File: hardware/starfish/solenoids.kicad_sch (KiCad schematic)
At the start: 8 parts, among them J1201 Solenoid, U1201 DRV120PWR

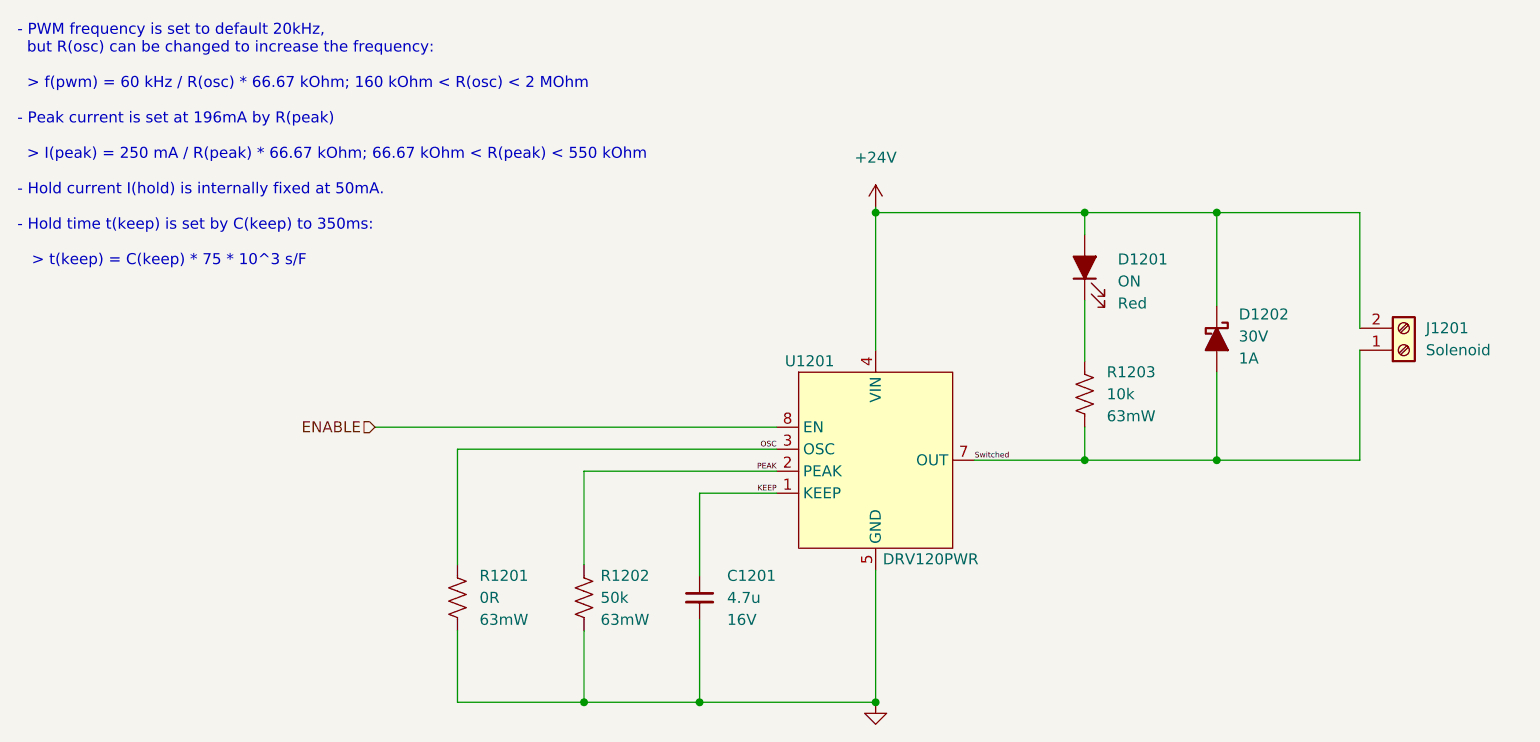
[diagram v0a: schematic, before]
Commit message: Mostly finished starfish schematic, ready for layout!
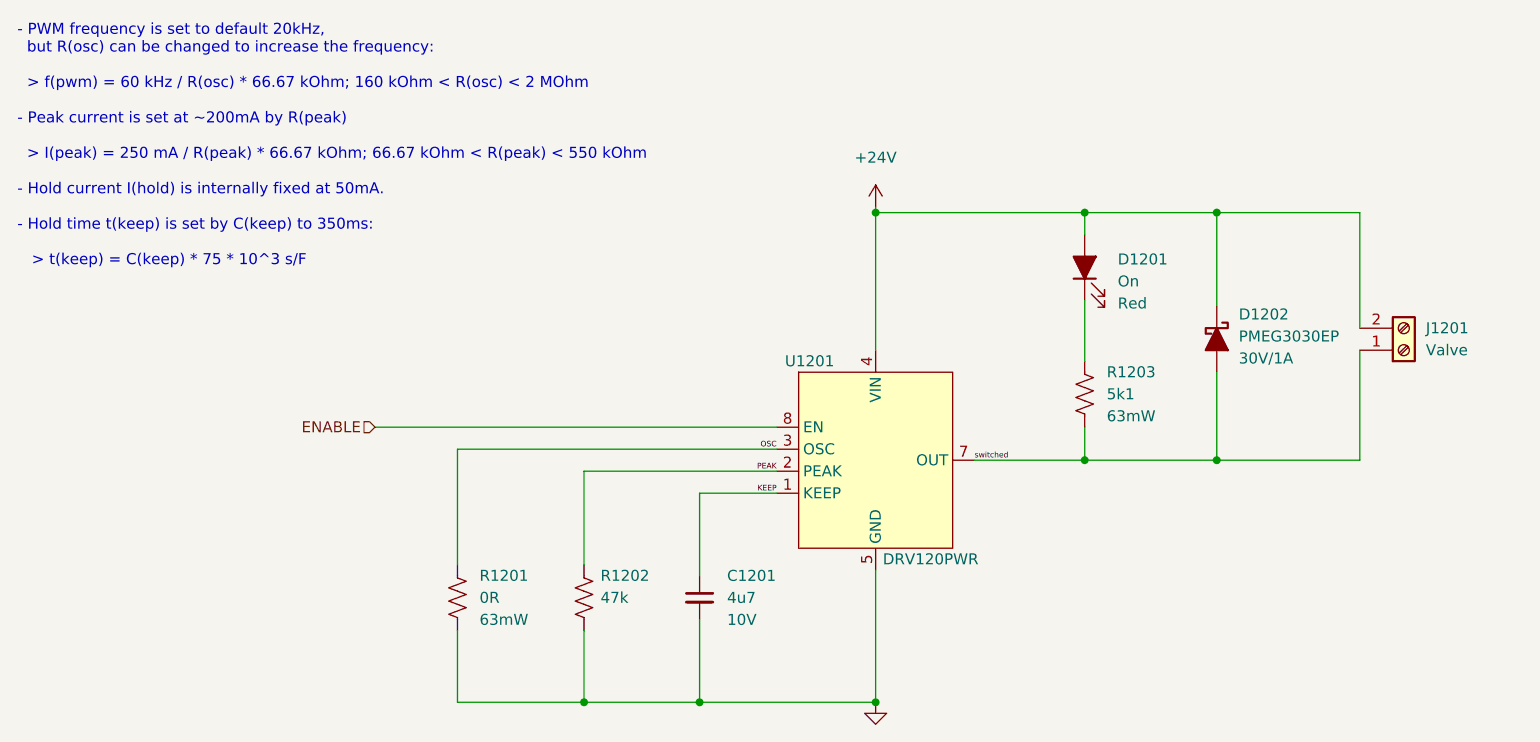
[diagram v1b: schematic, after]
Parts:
- C1201: value 4.7u -> 4u7; footprint Capacitor_SMD:C_0603_1608Metric_Pad1.08x0.95mm_HandSolder -> winterbloom:C_0603_HandSolder; Rating 16V -> 10V; mpn (none) -> CL10A475KP8NNNC
- D1201: value ON -> On
- D1202: value 30V -> PMEG3030EP; Rating 1A -> 30V/1A
- J1201: value Solenoid -> Valve
- R1201: footprint (none) -> winterbloom:R_0402_HandSolder
- R1202: value 50k -> 47k; footprint (none) -> winterbloom:R_0402_HandSolder; Field4 63mW -> (none); Rating (none) -> 63mW
- R1203: value 10k -> 5k1; footprint (none) -> winterbloom:R_0402_HandSolder; mpn (none) -> AC0603FR-075K1L
- U1201: MPN DRV120PWR -> (none)
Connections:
- net Switched renamed switched
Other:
- note added: "- PWM frequency is set to default 20kHz, but R(osc) can be changed to increase the frequency: > f(pwm) = 60 kHz / R(osc) * 66.67 kOhm; 160 kOhm < R(osc) < 2 MOhm - Peak current is set at ~200mA by R(peak) > I(peak) = 250 mA / R(peak) * 66.67 kOhm; 66.67 kOhm < R(peak) < 550 kOhm - Hold current I(hold) is internally fixed at 50mA. - Hold time t(keep) is set by C(keep) to 350ms: > t(keep) = C(keep)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"
- note removed: "- PWM frequency is set to default 20kHz, but R(osc) can be changed to increase the frequency: > f(pwm) = 60 kHz / R(osc) * 66.67 kOhm; 160 kOhm < R(osc) < 2 MOhm - Peak current is set at 196mA by R(peak) > I(peak) = 250 mA / R(peak) * 66.67 kOhm; 66.67 kOhm < R(peak) < 550 kOhm - Hold current I(hold) is internally fixed at 50mA. - Hold time t(keep) is set by C(keep) to 350ms: > t(keep) = C(keep) 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"
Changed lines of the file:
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@@
     (stroke (width 0) (type default) (color 0 0 0 0))
   )
-  (text "- PWM frequency is set to default 20kHz,\n  but R(osc) can be changed to increase the frequency:\n\n  > f(pwm) = 60 kHz / R(osc) * 66.67 kOhm; 160 kOhm < R(osc) < 2 MOhm\n\n- Peak current is set at 196mA by R(peak)\n\n  > I(peak) = 250 mA / R(peak) * 66.67 kOhm; 66.67 kOhm < R(peak) < 550 kOhm\n\n- Hold current I(hold) is internally fixed at 50mA.\n\n- Hold time t(keep) is set by C(keep) to 350ms:\n\n   > t(keep) = C(keep) * 75 * 10^3 s/F"
+  (text "- PWM frequency is set to default 20kHz,\n  but R(osc) can be changed to increase the frequency:\n\n  > f(pwm) = 60 kHz / R(osc) * 66.67 kOhm; 160 kOhm < R(osc) < 2 MOhm\n\n- Peak current is set at ~200mA by R(peak)\n\n  > I(peak) = 250 mA / R(peak) * 66.67 kOhm; 66.67 kOhm < R(peak) < 550 kOhm\n\n- Hold current I(hold) is internally fixed at 50mA.\n\n- Hold time t(keep) is set by C(keep) to 350ms:\n\n   > t(keep) = C(keep) * 75 * 10^3 s/F"
     (at 40.005 76.2 0)
     (effects (font (size 1.27 1.27)) (justify left bottom))
   )
-  (label "Switched" (at 150.495 98.425 0)
+  (label "switched" (at 150.495 98.425 0)
     (effects (font (size 0.64 0.64)) (justify left bottom))
   )
@@
       (effects (font (size 1.27 1.27)) (justify left))
     )
-    (property "Value" "Solenoid" (id 1) (at 202.565 85.725 0)
+    (property "Value" "Valve" (id 1) (at 202.565 85.725 0)
       (effects (font (size 1.27 1.27)) (justify left))
     )
@@
       (effects (font (size 1.27 1.27)) hide)
     )
-    (property "MPN" "DRV120PWR" (id 5) (at 158.115 110.49 0)
+    (property "MPN" "" (id 5) (at 158.115 110.49 0)
       (effects (font (size 1.27 1.27)) hide)
     )
@@
       (effects (font (size 1.27 1.27)) (justify right))
     )
-    (property "Value" "ON" (id 1) (at 167.005 77.7874 90)
+    (property "Value" "On" (id 1) (at 167.005 77.7874 90)
       (effects (font (size 1.27 1.27)) (justify right))
     )
@@
       (effects (font (size 1.27 1.27)) (justify left))
     )
-    (property "Value" "4.7u" (id 1) (at 121.92 114.3062 0)
-      (effects (font (size 1.27 1.27)) (justify left))
-    )
-    (property "Footprint" "Capacitor_SMD:C_0603_1608Metric_Pad1.08x0.95mm_HandSolder" (id 2) (at 118.745 114.3 0)
+    (property "Value" "4u7" (id 1) (at 121.92 114.3062 0)
+      (effects (font (size 1.27 1.27)) (justify left))
+    )
+    (property "Footprint" "winterbloom:C_0603_HandSolder" (id 2) (at 118.745 114.3 0)
       (effects (font (size 1.27 1.27)) hide)
     )
@@
       (effects (font (size 1.27 1.27)) hide)
     )
-    (property "Rating" "16V" (id 4) (at 121.92 116.8462 0)
-      (effects (font (size 1.27 1.27)) (justify left))
+    (property "Rating" "10V" (id 4) (at 121.92 116.8462 0)
+      (effects (font (size 1.27 1.27)) (justify left))
+    )
+    (property "mpn" "CL10A475KP8NNNC" (id 5) (at 118.745 114.3 0)
+      (effects (font (size 1.27 1.27)) hide)
     )
     (pin "1")
@@
       (effects (font (size 1.27 1.27)) (justify right))
     )
-    (property "Footprint" "" (id 2) (at 89.789 114.046 90)
+    (property "Footprint" "winterbloom:R_0402_HandSolder" (id 2) (at 89.789 114.046 90)
       (effects (font (size 1.27 1.27)) hide)
     )
@@
       (effects (font (size 1.27 1.27)) (justify right))
     )
-    (property "Value" "50k" (id 1) (at 107.315 114.2999 0)
-      (effects (font (size 1.27 1.27)) (justify right))
-    )
-    (property "Footprint" "" (id 2) (at 104.394 114.046 90)
+    (property "Value" "47k" (id 1) (at 107.315 114.2999 0)
+      (effects (font (size 1.27 1.27)) (justify right))
+    )
+    (property "Footprint" "winterbloom:R_0402_HandSolder" (id 2) (at 104.394 114.046 90)
       (effects (font (size 1.27 1.27)) hide)
     )
@@
       (effects (font (size 1.27 1.27)) hide)
     )
-    (property "Field4" "63mW" (id 4) (at 107.315 116.8399 0)
-      (effects (font (size 1.27 1.27)) (justify right))
+    (property "Field4" "" (id 4) (at 107.315 116.8399 0)
+      (effects (font (size 1.27 1.27)) (justify right))
+    )
+    (property "Rating" "63mW" (id 5) (at 105.41 114.3 0)
+      (effects (font (size 1.27 1.27)) hide)
     )
     (pin "1")
@@
       (effects (font (size 1.27 1.27)) (justify left))
     )
-    (property "Value" "30V" (id 1) (at 180.975 84.1374 90)
+    (property "Value" "PMEG3030EP" (id 1) (at 180.975 84.1374 90)
       (effects (font (size 1.27 1.27)) (justify left))
     )
@@
       (effects (font (size 1.27 1.27)) hide)
     )
-    (property "Rating" "1A" (id 4) (at 180.975 86.6774 90)
+    (property "Rating" "30V/1A" (id 4) (at 180.975 86.6774 90)
       (effects (font (size 1.27 1.27)) (justify left))
     )
@@
       (effects (font (size 1.27 1.27)) (justify left))
     )
-    (property "Value" "10k" (id 1) (at 165.735 90.8049 0)
-      (effects (font (size 1.27 1.27)) (justify left))
-    )
-    (property "Footprint" "" (id 2) (at 164.211 91.059 90)
+    (property "Value" "5k1" (id 1) (at 165.735 90.8049 0)
+      (effects (font (size 1.27 1.27)) (justify left))
+    )
+    (property "Footprint" "winterbloom:R_0402_HandSolder" (id 2) (at 164.211 91.059 90)
       (effects (font (size 1.27 1.27)) hide)
     )
@@
       (effects (font (size 1.27 1.27)) hide)
     )
-    (property "mpn" "" (id 4) (at 163.195 90.805 0)
-      (effects (font (size 1.27 1.27)) hide)
-    )
+    (property "mpn" "AC0603FR-075K1L" (id 4) (at 163.195 90.805 0)
+      (effects (font (size 1.27 1.27)) hide)
+    )

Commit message: First pass at layout and routing
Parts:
- added C1202: 100n, winterbloom:C_0603_HandSolder, symbol Device:C_Small
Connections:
- net +24V: now also C1202.1
- net GND: now also C1202.2
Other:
- moved on the sheet: D1201, D1202, J1201, R1203

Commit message: Layout and routing mostly done! Just gotta make it prettier!
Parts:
- D1202: footprint Diode_SMD:D_SOD-128 -> winterbloom:D_SOD-128
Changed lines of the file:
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@@
       (effects (font (size 1.27 1.27)) (justify left))
     )
-    (property "Footprint" "Diode_SMD:D_SOD-128" (id 2) (at 182.88 84.455 0)
+    (property "Footprint" "winterbloom:D_SOD-128" (id 2) (at 182.88 84.455 0)
       (effects (font (size 1.27 1.27)) hide)
     )

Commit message: Run through purchasing, update some cap sizes
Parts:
- D1202: mpn (none) -> PMEG3030EP,115
- R1201: mpn (none) -> RMCF0402ZT0R00
- R1202: mpn (none) -> RC0402FR-0747KL
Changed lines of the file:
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@@
       (effects (font (size 1.27 1.27)) (justify right))
+    )
+    (property "mpn" "RMCF0402ZT0R00" (id 5) (at 90.805 114.3 0)
+      (effects (font (size 1.27 1.27)) hide)
     )
     (pin "1")
@@
       (effects (font (size 1.27 1.27)) hide)
     )
+    (property "mpn" "RC0402FR-0747KL" (id 6) (at 105.41 114.3 0)
+      (effects (font (size 1.27 1.27)) hide)
+    )
     (pin "1")
     (pin "2")
@@
       (effects (font (size 1.27 1.27)) (justify left))
     )
+    (property "mpn" "PMEG3030EP,115" (id 5) (at 182.88 84.455 0)
+      (effects (font (size 1.27 1.27)) hide)
+    )
     (pin "1")
